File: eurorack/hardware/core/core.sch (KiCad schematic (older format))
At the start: 48 parts, among them J1 ConnNW, J2 ConnSW, J3 ConnNE, J4 ConnSE, J5 Power, J6 SWD, SW1 Reset, SW2 Boot0, U1 STM32F427VGT6, U2 TLV320AIC23BPW, U3 LM1117F-3.3, U4 LM4040C10IDBZR, Y1 Crystal

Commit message: Wire up power section
Signed-off-by: Petr Horacek <hrck@protonmail.com>
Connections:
- wire segments 215 -> 224
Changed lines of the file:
@@
 L Connector_Generic:Conn_01x10 J1
 U 1 1 60AE94CD
-P 9025 4375
-F 0 "J1" H 9105 4367 50  0000 L CNN
-F 1 "ConnNW" H 9105 4276 50  0000 L CNN
-F 2 "Connector_PinHeader_2.54mm:PinHeader_1x10_P2.54mm_Vertical" H 9025 4375 50  0001 C CNN
-F 3 "~" H 9025 4375 50  0001 C CNN
-	1    9025 4375
+P 9400 4375
+F 0 "J1" H 9350 5000 50  0000 L CNN
+F 1 "ConnNW" H 9275 4900 50  0000 L CNN
+F 2 "Connector_PinHeader_2.54mm:PinHeader_1x10_P2.54mm_Vertical" H 9400 4375 50  0001 C CNN
+F 3 "~" H 9400 4375 50  0001 C CNN
+	1    9400 4375
 	1    0    0    -1
 $EndComp
@@
 L Connector_Generic:Conn_01x10 J2
 U 1 1 60AEC1D4
-P 9025 5725
-F 0 "J2" H 9105 5717 50  0000 L CNN
-F 1 "ConnSW" H 9105 5626 50  0000 L CNN
-F 2 "Connector_PinHeader_2.54mm:PinHeader_1x10_P2.54mm_Vertical" H 9025 5725 50  0001 C CNN
-F 3 "~" H 9025 5725 50  0001 C CNN
-	1    9025 5725
+P 9400 5725
+F 0 "J2" H 9350 6325 50  0000 L CNN
+F 1 "ConnSW" H 9275 6250 50  0000 L CNN
+F 2 "Connector_PinHeader_2.54mm:PinHeader_1x10_P2.54mm_Vertical" H 9400 5725 50  0001 C CNN
+F 3 "~" H 9400 5725 50  0001 C CNN
+	1    9400 5725
 	1    0    0    -1
 $EndComp
@@
 U 1 1 60AED02D
 P 10750 4375
-F 0 "J3" H 10830 4367 50  0000 L CNN
-F 1 "ConnNE" H 10830 4276 50  0000 L CNN
+F 0 "J3" H 10700 5000 50  0000 L CNN
+F 1 "ConnNE" H 10650 4900 50  0000 L CNN
 F 2 "Connector_PinHeader_2.54mm:PinHeader_1x10_P2.54mm_Vertical" H 10750 4375 50  0001 C CNN
 F 3 "~" H 10750 4375 50  0001 C CNN
@@
 U 1 1 60AED5FD
 P 10750 5725
-F 0 "J4" H 10830 5717 50  0000 L CNN
-F 1 "ConnSE" H 10830 5626 50  0000 L CNN
+F 0 "J4" H 10700 6325 50  0000 L CNN
+F 1 "ConnSE" H 10650 6250 50  0000 L CNN
 F 2 "Connector_PinHeader_2.54mm:PinHeader_1x10_P2.54mm_Vertical" H 10750 5725 50  0001 C CNN
 F 3 "~" H 10750 5725 50  0001 C CNN
@@
 Text GLabel 4450 4450 2    50   Input ~ 0
 I2S_DOUT
+$Comp
+L power:GND #PWR0117
+U 1 1 6187E70C
+P 9200 3975
+F 0 "#PWR0117" H 9200 3725 50  0001 C CNN
+F 1 "GND" V 9200 3775 50  0000 C CNN
+F 2 "" H 9200 3975 50  0001 C CNN
+F 3 "" H 9200 3975 50  0001 C CNN
+	1    9200 3975
+	0    1    1    0
+$EndComp
+Wire Wire Line
+	9200 3975 10550 3975
+Wire Wire Line
+	9200 4075 10550 4075
+Wire Wire Line
+	10550 4175 9200 4175
+Wire Wire Line
+	9200 4275 10550 4275
+Wire Wire Line
+	10550 4375 9200 4375
+Wire Wire Line
+	9200 4475 10550 4475
+Connection ~ 9200 3975
+$Comp
+L power:VCC #PWR0118
+U 1 1 6190EBA1
+P 9050 4075
+F 0 "#PWR0118" H 9050 3925 50  0001 C CNN
+F 1 "VCC" V 9050 4275 50  0000 C CNN
+F 2 "" H 9050 4075 50  0001 C CNN
+F 3 "" H 9050 4075 50  0001 C CNN
+	1    9050 4075
+	0    -1   -1   0
+$EndComp
+Wire Wire Line
+	9050 4075 9200 4075
+Connection ~ 9200 4075
+$Comp
+L power:VEE #PWR0119
+U 1 1 61957B12
+P 9200 4175
+F 0 "#PWR0119" H 9200 4025 50  0001 C CNN
+F 1 "VEE" V 9200 4375 50  0000 C CNN
+F 2 "" H 9200 4175 50  0001 C CNN
+F 3 "" H 9200 4175 50  0001 C CNN
+	1    9200 4175
+	0    -1   -1   0
+$EndComp
+$Comp
+L power:+3.3V #PWR0120
+U 1 1 6196923E
+P 9200 4375
+F 0 "#PWR0120" H 9200 4225 50  0001 C CNN
+F 1 "+3.3V" V 9200 4625 50  0000 C CNN
+F 2 "" H 9200 4375 50  0001 C CNN
+F 3 "" H 9200 4375 50  0001 C CNN
+	1    9200 4375
+	0    -1   -1   0
+$EndComp
+Connection ~ 9200 4275
+$Comp
+L power:+3.3VA #PWR0121
+U 1 1 6196A060
+P 9025 4475
+F 0 "#PWR0121" H 9025 4325 50  0001 C CNN
+F 1 "+3.3VA" V 9025 4750 50  0000 C CNN
+F 2 "" H 9025 4475 50  0001 C CNN
+F 3 "" H 9025 4475 50  0001 C CNN
+	1    9025 4475
+	0    -1   -1   0
+$EndComp
+$Comp
+L power:-10V #PWR?
+U 1 1 619A4697
+P 9050 4275
+F 0 "#PWR?" H 9050 4375 50  0001 C CNN
+F 1 "-10V" V 9065 4403 50  0000 L CNN
+F 2 "" H 9050 4275 50  0001 C CNN
+F 3 "" H 9050 4275 50  0001 C CNN
+	1    9050 4275
+	0    -1   -1   0
+$EndComp
+Wire Wire Line
+	9050 4275 9200 4275
+Connection ~ 9200 4175
+Connection ~ 9200 4375
+Wire Wire Line
+	9025 4475 9200 4475
+Connection ~ 9200 4475
 $EndSCHEMATC

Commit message: Wire up DAC
Signed-off-by: Petr Horacek <hrck@protonmail.com>
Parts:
- removed J1: ConnNW, Connector_PinHeader_2.54mm:PinHeader_1x10_P2.54mm_Vertical, symbol Connector_Generic:Conn_01x10
- removed J2: ConnSW, Connector_PinHeader_2.54mm:PinHeader_1x10_P2.54mm_Vertical, symbol Connector_Generic:Conn_01x10
- removed J3: ConnNE, Connector_PinHeader_2.54mm:PinHeader_1x10_P2.54mm_Vertical, symbol Connector_Generic:Conn_01x10
- removed J4: ConnSE, Connector_PinHeader_2.54mm:PinHeader_1x10_P2.54mm_Vertical, symbol Connector_Generic:Conn_01x10
- added J1: ConnNW, Connector_PinHeader_2.54mm:PinHeader_1x14_P2.54mm_Vertical, symbol Connector_Generic:Conn_01x14
- added J2: ConnSW, Connector_PinHeader_2.54mm:PinHeader_1x06_P2.54mm_Vertical, symbol Connector_Generic:Conn_01x06
- added J3: ConnNE, Connector_PinHeader_2.54mm:PinHeader_1x14_P2.54mm_Vertical, symbol Connector_Generic:Conn_01x14
- added J4: ConnSE, Connector_PinHeader_2.54mm:PinHeader_1x06_P2.54mm_Vertical, symbol Connector_Generic:Conn_01x06
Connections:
- net labels added: LIN, LOUT, RIN, ROUT
- wire segments 224 -> 227
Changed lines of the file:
@@
-$EndComp
-$Comp
-L Connector_Generic:Conn_01x10 J1
-U 1 1 60AE94CD
-P 9400 4375
-F 0 "J1" H 9350 5000 50  0000 L CNN
-F 1 "ConnNW" H 9275 4900 50  0000 L CNN
-F 2 "Connector_PinHeader_2.54mm:PinHeader_1x10_P2.54mm_Vertical" H 9400 4375 50  0001 C CNN
-F 3 "~" H 9400 4375 50  0001 C CNN
-	1    9400 4375
-	1    0    0    -1
-$EndComp
-$Comp
-L Connector_Generic:Conn_01x10 J2
-U 1 1 60AEC1D4
-P 9400 5725
-F 0 "J2" H 9350 6325 50  0000 L CNN
-F 1 "ConnSW" H 9275 6250 50  0000 L CNN
-F 2 "Connector_PinHeader_2.54mm:PinHeader_1x10_P2.54mm_Vertical" H 9400 5725 50  0001 C CNN
-F 3 "~" H 9400 5725 50  0001 C CNN
-	1    9400 5725
-	1    0    0    -1
-$EndComp
-$Comp
-L Connector_Generic:Conn_01x10 J3
-U 1 1 60AED02D
-P 10750 4375
-F 0 "J3" H 10700 5000 50  0000 L CNN
-F 1 "ConnNE" H 10650 4900 50  0000 L CNN
-F 2 "Connector_PinHeader_2.54mm:PinHeader_1x10_P2.54mm_Vertical" H 10750 4375 50  0001 C CNN
-F 3 "~" H 10750 4375 50  0001 C CNN
-	1    10750 4375
-	1    0    0    -1
-$EndComp
-$Comp
-L Connector_Generic:Conn_01x10 J4
-U 1 1 60AED5FD
-P 10750 5725
-F 0 "J4" H 10700 6325 50  0000 L CNN
-F 1 "ConnSE" H 10650 6250 50  0000 L CNN
-F 2 "Connector_PinHeader_2.54mm:PinHeader_1x10_P2.54mm_Vertical" H 10750 5725 50  0001 C CNN
-F 3 "~" H 10750 5725 50  0001 C CNN
-	1    10750 5725
-	1    0    0    -1
 $EndComp
 $Comp
@@
 $EndComp
 Wire Wire Line
-	9200 3975 10550 3975
-Wire Wire Line
-	9200 4075 10550 4075
-Wire Wire Line
-	10550 4175 9200 4175
-Wire Wire Line
-	9200 4275 10550 4275
-Wire Wire Line
-	10550 4375 9200 4375
-Wire Wire Line
-	9200 4475 10550 4475
-Connection ~ 9200 3975
+	9200 3975 9225 3975
+Wire Wire Line
+	10550 4175 9225 4175
+Wire Wire Line
+	10550 4375 9225 4375
 $Comp
 L power:VCC #PWR0118
@@
 	0    -1   -1   0
 $EndComp
-Wire Wire Line
-	9050 4075 9200 4075
-Connection ~ 9200 4075
 $Comp
 L power:VEE #PWR0119
@@
 	0    -1   -1   0
 $EndComp
-Connection ~ 9200 4275
 $Comp
 L power:+3.3VA #PWR0121
@@
 $EndComp
 $Comp
-L power:-10V #PWR?
+L power:-10V #PWR0122
 U 1 1 619A4697
 P 9050 4275
-F 0 "#PWR?" H 9050 4375 50  0001 C CNN
+F 0 "#PWR0122" H 9050 4375 50  0001 C CNN
 F 1 "-10V" V 9065 4403 50  0000 L CNN
 F 2 "" H 9050 4275 50  0001 C CNN
@@
 	0    -1   -1   0
 $EndComp
-Wire Wire Line
-	9050 4275 9200 4275
-Connection ~ 9200 4175
-Connection ~ 9200 4375
-Wire Wire Line
-	9025 4475 9200 4475
-Connection ~ 9200 4475
+Text GLabel 7875 2950 2    50   Input ~ 0
+LOUT
+Text GLabel 7875 3050 2    50   Input ~ 0
+ROUT
+Text GLabel 7875 3550 2    50   Input ~ 0
+LIN
+Text GLabel 7875 3650 2    50   Input ~ 0
+RIN
+$Comp
+L Connector_Generic:Conn_01x14 J1
+U 1 1 61A20C8E
+P 9425 4575
+F 0 "J1" H 9375 5375 50  0000 L CNN
+F 1 "ConnNW" H 9275 5300 50  0000 L CNN
+F 2 "Connector_PinHeader_2.54mm:PinHeader_1x14_P2.54mm_Vertical" H 9425 4575 50  0001 C CNN
+F 3 "~" H 9425 4575 50  0001 C CNN
+	1    9425 4575
+	1    0    0    -1
+$EndComp
+$Comp
+L Connector_Generic:Conn_01x14 J3
+U 1 1 61A240F0
+P 10750 4575
+F 0 "J3" H 10700 5375 50  0000 L CNN
+F 1 "ConnNE" H 10600 5300 50  0000 L CNN
+F 2 "Connector_PinHeader_2.54mm:PinHeader_1x14_P2.54mm_Vertical" H 10750 4575 50  0001 C CNN
+F 3 "~" H 10750 4575 50  0001 C CNN
+	1    10750 4575
+	1    0    0    -1
+$EndComp
+Wire Wire Line
+	9050 4075 9225 4075
+Wire Wire Line
+	9050 4275 9225 4275
+Wire Wire Line
+	9025 4475 9225 4475
+Connection ~ 9225 3975
+Wire Wire Line
+	9225 3975 10550 3975
+Connection ~ 9225 4075
+Wire Wire Line
+	9225 4075 10550 4075
+Connection ~ 9225 4175
+Wire Wire Line
+	9225 4175 9200 4175
+Connection ~ 9225 4275
+Wire Wire Line
+	9225 4275 10550 4275
+Connection ~ 9225 4375
+Wire Wire Line
+	9225 4375 9200 4375
+Connection ~ 9225 4475
+Wire Wire Line
+	9225 4475 10550 4475
+$Comp
+L Connector_Generic:Conn_01x06 J2
+U 1 1 61A34DEB
+P 9425 6000
+F 0 "J2" H 9375 6400 50  0000 L CNN
+F 1 "ConnSW" H 9275 6325 50  0000 L CNN
+F 2 "Connector_PinHeader_2.54mm:PinHeader_1x06_P2.54mm_Vertical" H 9425 6000 50  0001 C CNN
+F 3 "~" H 9425 6000 50  0001 C CNN
+	1    9425 6000
+	1    0    0    -1
+$EndComp
+$Comp
+L Connector_Generic:Conn_01x06 J4
+U 1 1 61A3654B
+P 10750 6000
+F 0 "J4" H 10700 6400 50  0000 L CNN
+F 1 "ConnSE" H 10600 6325 50  0000 L CNN
+F 2 "Connector_PinHeader_2.54mm:PinHeader_1x06_P2.54mm_Vertical" H 10750 6000 50  0001 C CNN
+F 3 "~" H 10750 6000 50  0001 C CNN
+	1    10750 6000
+	1    0    0    -1
+$EndComp
+Text GLabel 9225 4675 0    50   Input ~ 0
+LIN
+Text GLabel 9225 4575 0    50   Input ~ 0
+RIN
+Text GLabel 10550 4575 0    50   Input ~ 0
+LOUT
+Text GLabel 10550 4675 0    50   Input ~ 0
+ROUT
 $EndSCHEMATC

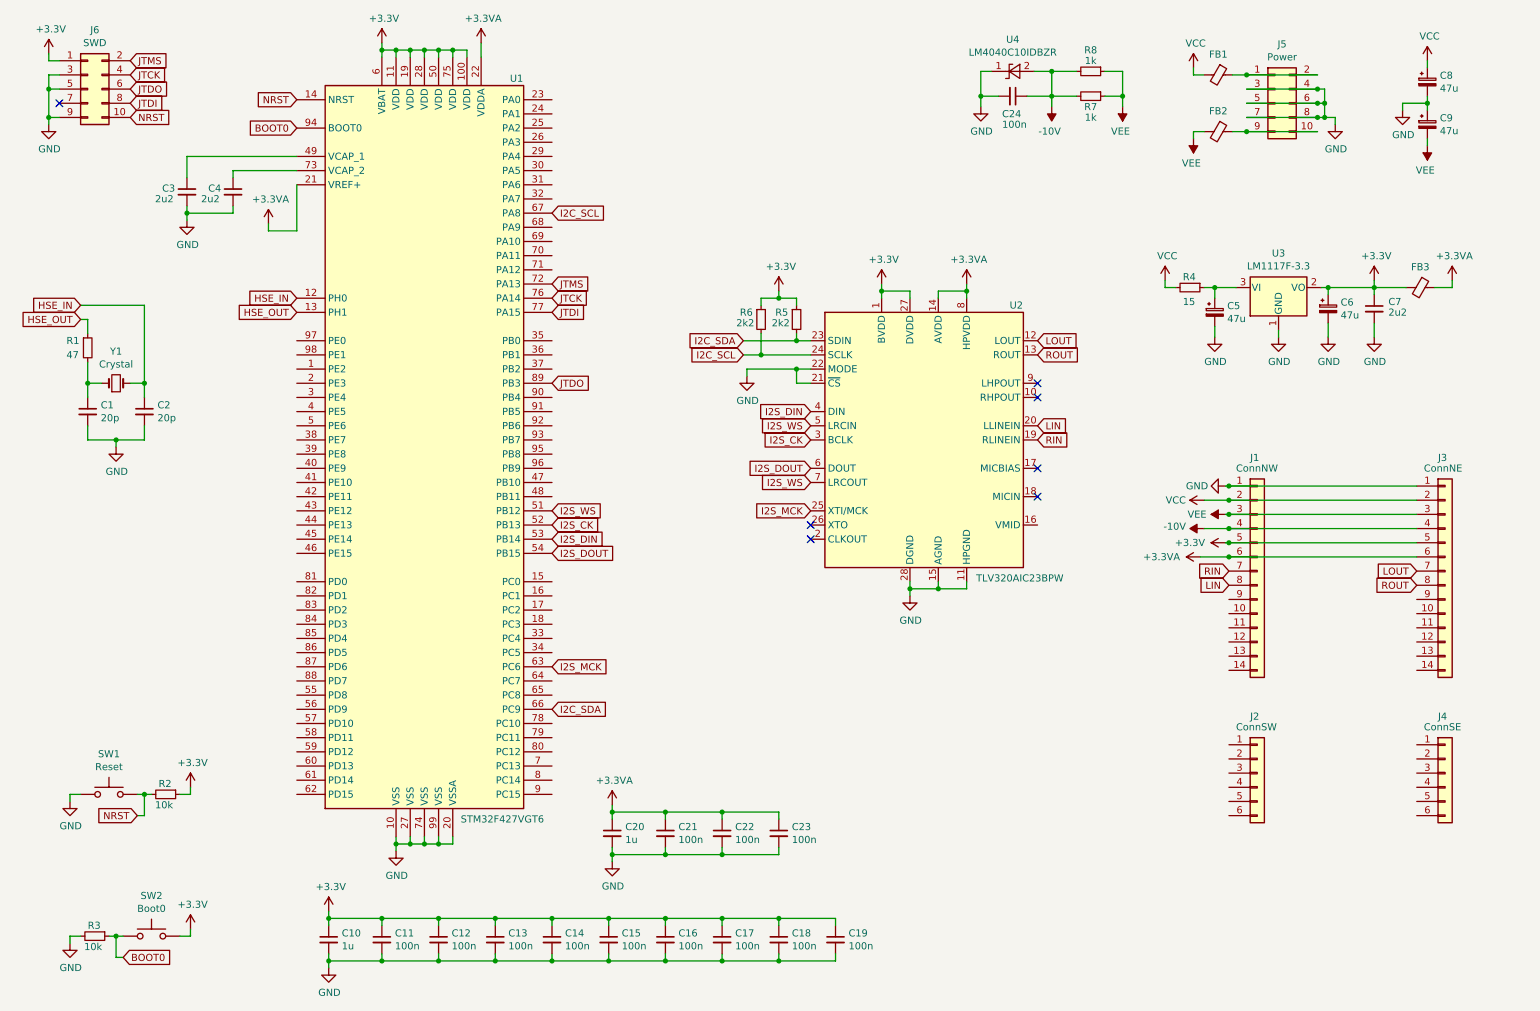
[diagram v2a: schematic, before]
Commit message: Wire up all pins
Signed-off-by: Petr Horacek <hrck@protonmail.com>
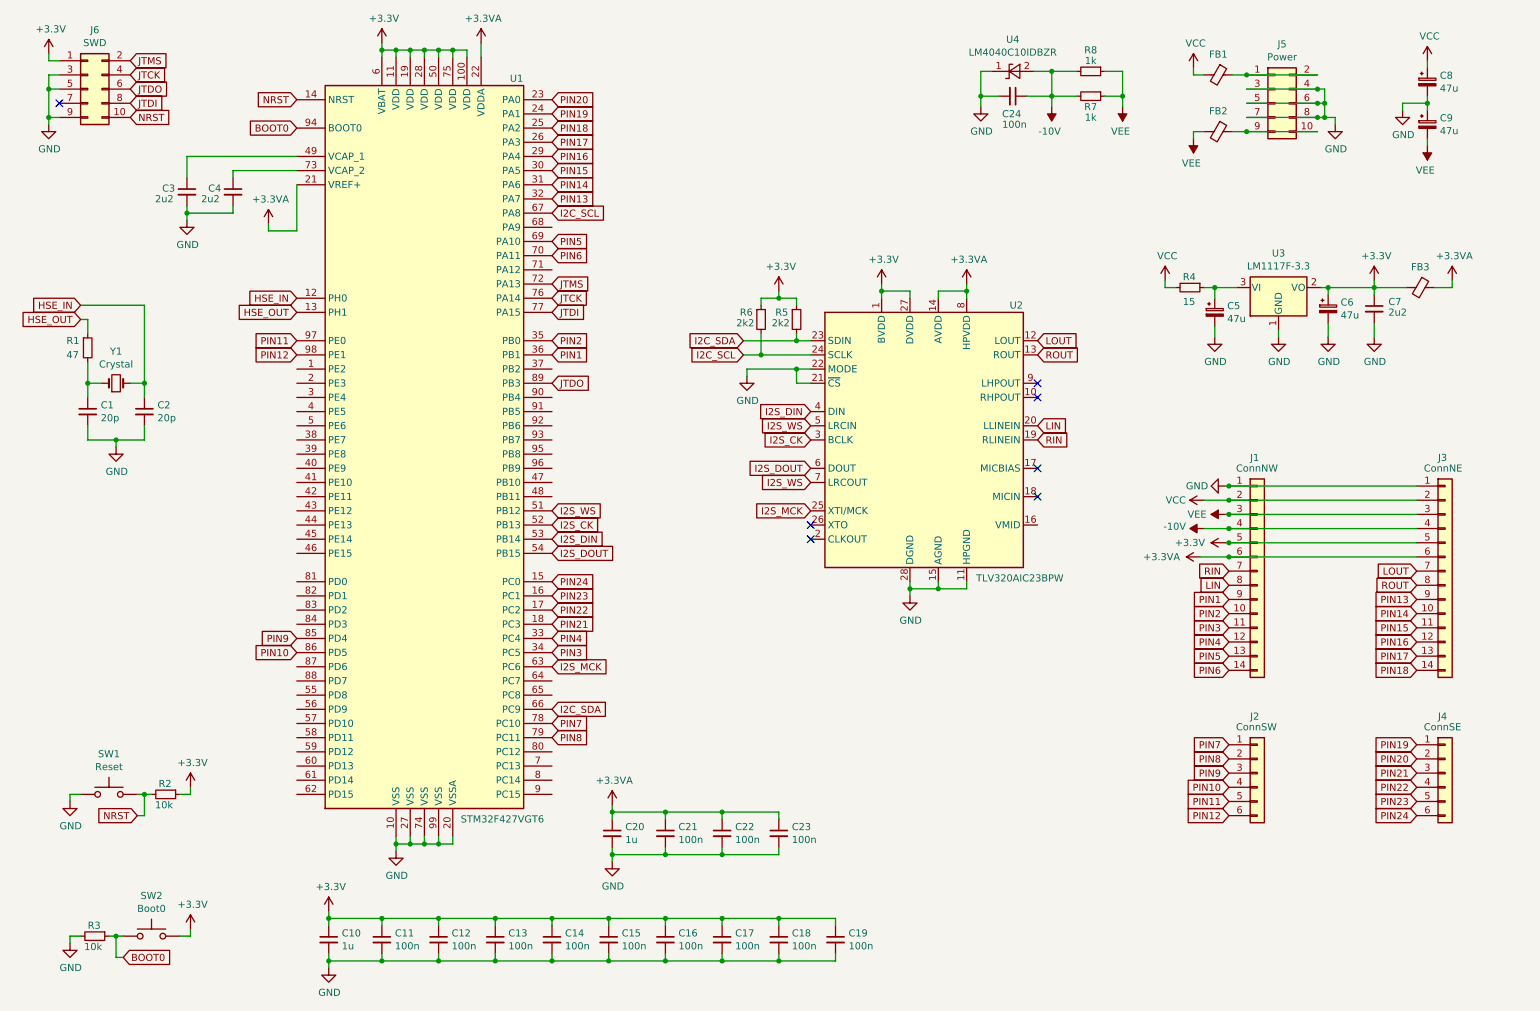
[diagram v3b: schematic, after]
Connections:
- net PIN24: now reaches U1.15 (PC0)
- net PIN24: now also J4.6 (Pin_6)
- net PIN23: now reaches U1.16 (PC1)
- net PIN23: now also J4.5 (Pin_5)
- net PIN22: now reaches U1.17 (PC2)
- net PIN22: now also J4.4 (Pin_4)
- net PIN21: now reaches U1.18 (PC3)
- net PIN21: now also J4.3 (Pin_3)
- net PIN20: now reaches U1.23 (PA0)
- net PIN20: now also J4.2 (Pin_2)
- net PIN19: now reaches U1.24 (PA1)
- net PIN19: now also J4.1 (Pin_1)
- net PIN18: now reaches U1.25 (PA2)
- net PIN18: now also J3.14 (Pin_14)
- net PIN17: now reaches U1.26 (PA3)
- net PIN17: now also J3.13 (Pin_13)
- net PIN16: now reaches U1.29 (PA4)
- net PIN16: now also J3.12 (Pin_12)
- net PIN15: now reaches U1.30 (PA5)
- net PIN15: now also J3.11 (Pin_11)
- net PIN14: now reaches U1.31 (PA6)
- net PIN14: now also J3.10 (Pin_10)
- net PIN13: now reaches U1.32 (PA7)
- net PIN13: now also J3.9 (Pin_9)
- net PIN4: now reaches U1.33 (PC4)
- net PIN4: now also J1.12 (Pin_12)
- net PIN3: now reaches U1.34 (PC5)
- net PIN3: now also J1.11 (Pin_11)
- net PIN2: now reaches U1.35 (PB0)
- net PIN2: now also J1.10 (Pin_10)
- net PIN1: now reaches U1.36 (PB1)
- net PIN1: now also J1.9 (Pin_9)
- net PIN5: now reaches U1.69 (PA10)
- net PIN5: now also J1.13 (Pin_13)
- net PIN6: now reaches U1.70 (PA11)
- net PIN6: now also J1.14 (Pin_14)
- net PIN7: now reaches U1.78 (PC10)
- net PIN7: now also J2.1 (Pin_1)
- net PIN8: now reaches U1.79 (PC11)
- net PIN8: now also J2.2 (Pin_2)
- net PIN9: now reaches U1.85 (PD4)
- net PIN9: now also J2.3 (Pin_3)
- net PIN10: now reaches U1.86 (PD5)
- net PIN10: now also J2.4 (Pin_4)
- net PIN11: now reaches U1.97 (PE0)
- net PIN11: now also J2.5 (Pin_5)
- net PIN12: now reaches U1.98 (PE1)
- net PIN12: now also J2.6 (Pin_6)
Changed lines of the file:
@@
 Text GLabel 10550 4675 0    50   Input ~ 0
 ROUT
+Text GLabel 10550 6300 0    50   Input ~ 0
+PIN24
+Text GLabel 10550 6200 0    50   Input ~ 0
+PIN23
+Text GLabel 10550 6100 0    50   Input ~ 0
+PIN22
+Text GLabel 10550 6000 0    50   Input ~ 0
+PIN21
+Text GLabel 10550 5900 0    50   Input ~ 0
+PIN20
+Text GLabel 10550 5800 0    50   Input ~ 0
+PIN19
+Text GLabel 10550 5275 0    50   Input ~ 0
+PIN18
+Text GLabel 10550 5175 0    50   Input ~ 0
+PIN17
+Text GLabel 10550 5075 0    50   Input ~ 0
+PIN16
+Text GLabel 10550 4975 0    50   Input ~ 0
+PIN15
+Text GLabel 10550 4875 0    50   Input ~ 0
+PIN14
+Text GLabel 10550 4775 0    50   Input ~ 0
+PIN13
+Text GLabel 9225 4775 0    50   Input ~ 0
+PIN1
+Text GLabel 9225 4875 0    50   Input ~ 0
+PIN2
+Text GLabel 9225 4975 0    50   Input ~ 0
+PIN3
+Text GLabel 9225 5075 0    50   Input ~ 0
+PIN4
+Text GLabel 9225 5175 0    50   Input ~ 0
+PIN5
+Text GLabel 9225 5275 0    50   Input ~ 0
+PIN6
+Text GLabel 9225 5800 0    50   Input ~ 0
+PIN7
+Text GLabel 9225 5900 0    50   Input ~ 0
+PIN8
+Text GLabel 9225 6000 0    50   Input ~ 0
+PIN9
+Text GLabel 9225 6100 0    50   Input ~ 0
+PIN10
+Text GLabel 9225 6200 0    50   Input ~ 0
+PIN11
+Text GLabel 9225 6300 0    50   Input ~ 0
+PIN12
+Text GLabel 4450 4650 2    50   Input ~ 0
+PIN24
+Text GLabel 4450 4750 2    50   Input ~ 0
+PIN23
+Text GLabel 4450 4850 2    50   Input ~ 0
+PIN22
+Text GLabel 4450 4950 2    50   Input ~ 0
+PIN21
+Text GLabel 4450 1250 2    50   Input ~ 0
+PIN20
+Text GLabel 4450 1350 2    50   Input ~ 0
+PIN19
+Text GLabel 4450 1450 2    50   Input ~ 0
+PIN18
+Text GLabel 4450 1550 2    50   Input ~ 0
+PIN17
+Text GLabel 4450 1650 2    50   Input ~ 0
+PIN16
+Text GLabel 4450 1750 2    50   Input ~ 0
+PIN15
+Text GLabel 4450 1850 2    50   Input ~ 0
+PIN14
+Text GLabel 4450 1950 2    50   Input ~ 0
+PIN13
+Text GLabel 4450 3050 2    50   Input ~ 0
+PIN1
+Text GLabel 4450 2950 2    50   Input ~ 0
+PIN2
+Text GLabel 4450 5150 2    50   Input ~ 0
+PIN3
+Text GLabel 4450 5050 2    50   Input ~ 0
+PIN4
+Text GLabel 2650 3050 0    50   Input ~ 0
+PIN12
+Text GLabel 2650 2950 0    50   Input ~ 0
+PIN11
+Text GLabel 4450 5650 2    50   Input ~ 0
+PIN7
+Text GLabel 4450 5750 2    50   Input ~ 0
+PIN8
+Text GLabel 2650 5050 0    50   Input ~ 0
+PIN9
+Text GLabel 2650 5150 0    50   Input ~ 0
+PIN10
+Text GLabel 4450 2350 2    50   Input ~ 0
+PIN6
+Text GLabel 4450 2250 2    50   Input ~ 0
+PIN5
 $EndSCHEMATC
